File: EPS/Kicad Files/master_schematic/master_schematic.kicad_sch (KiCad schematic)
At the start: 2 parts

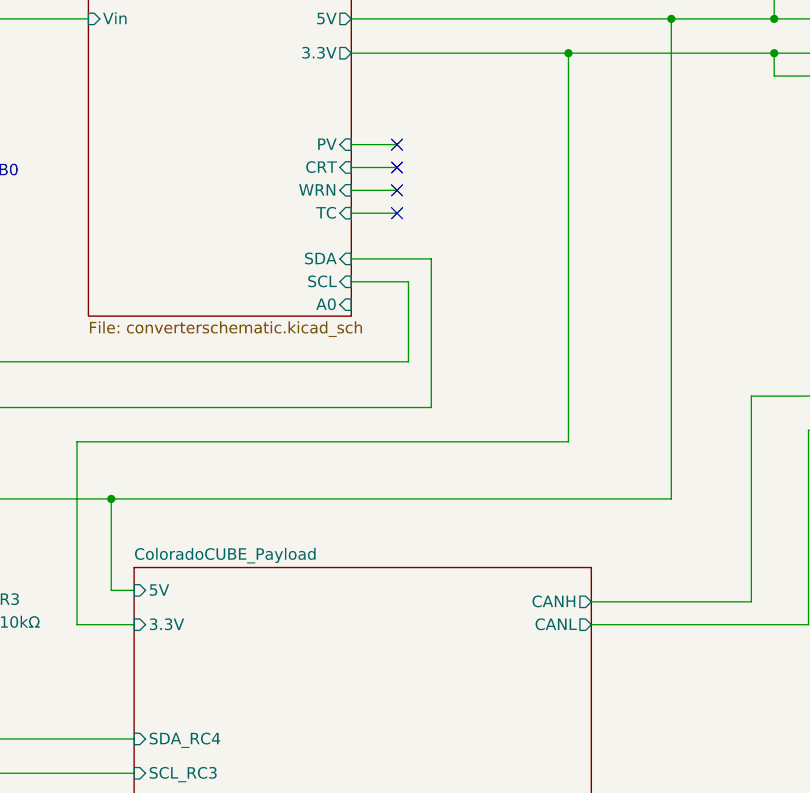
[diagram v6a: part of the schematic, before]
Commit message: EPS 2.0 update
added alert pins to microcontroller
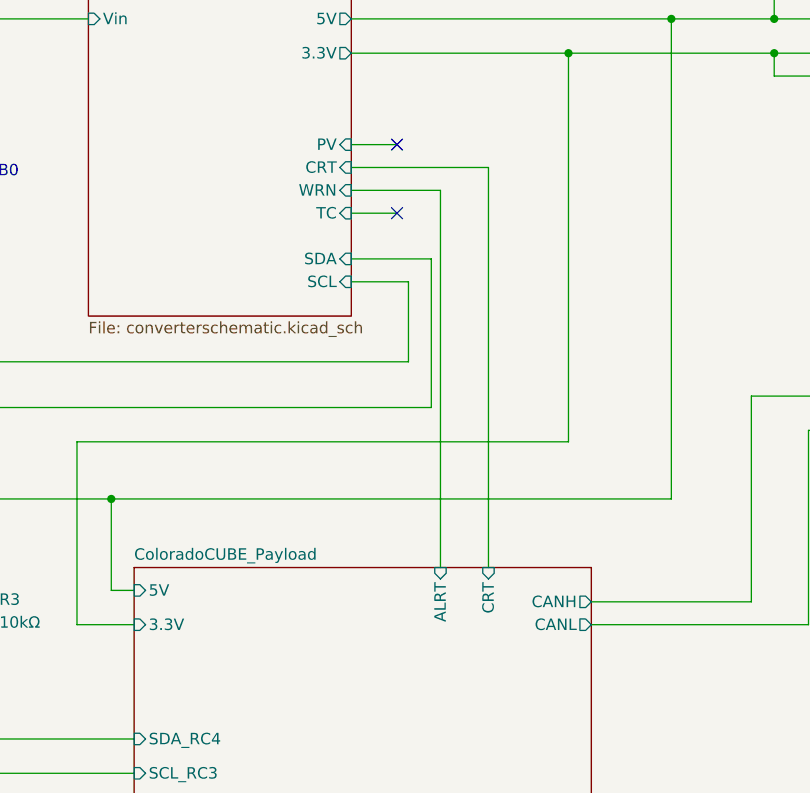
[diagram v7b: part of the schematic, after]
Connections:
- no-connect marks 9 -> 7
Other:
- sheet ColoradoCUBE_Payload ports: added ALRT, CRT; removed none
- sheet converterschematic ports: added none; removed A0
